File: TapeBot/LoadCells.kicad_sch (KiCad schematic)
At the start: 34 parts, among them Q2 MMBT4403

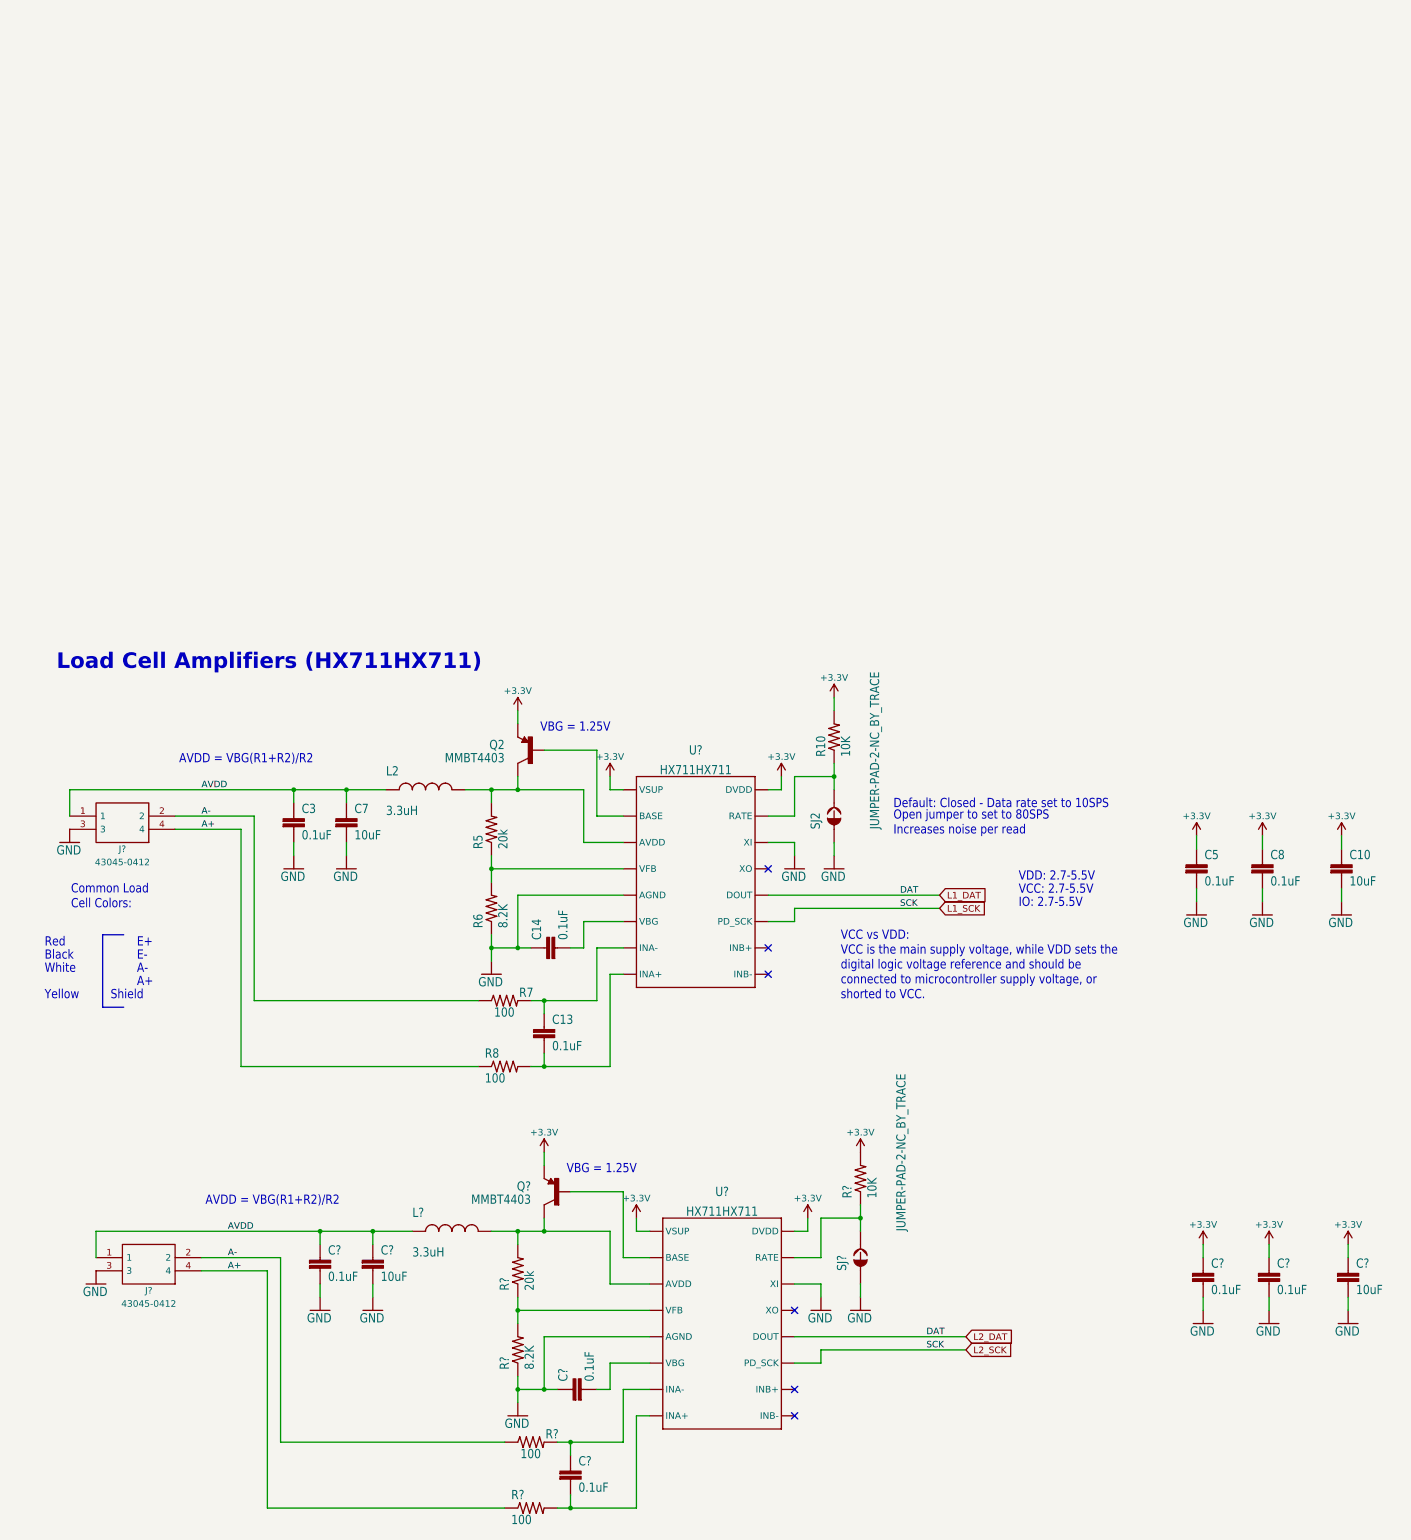
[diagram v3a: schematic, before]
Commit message: fixed footprints and 3d models
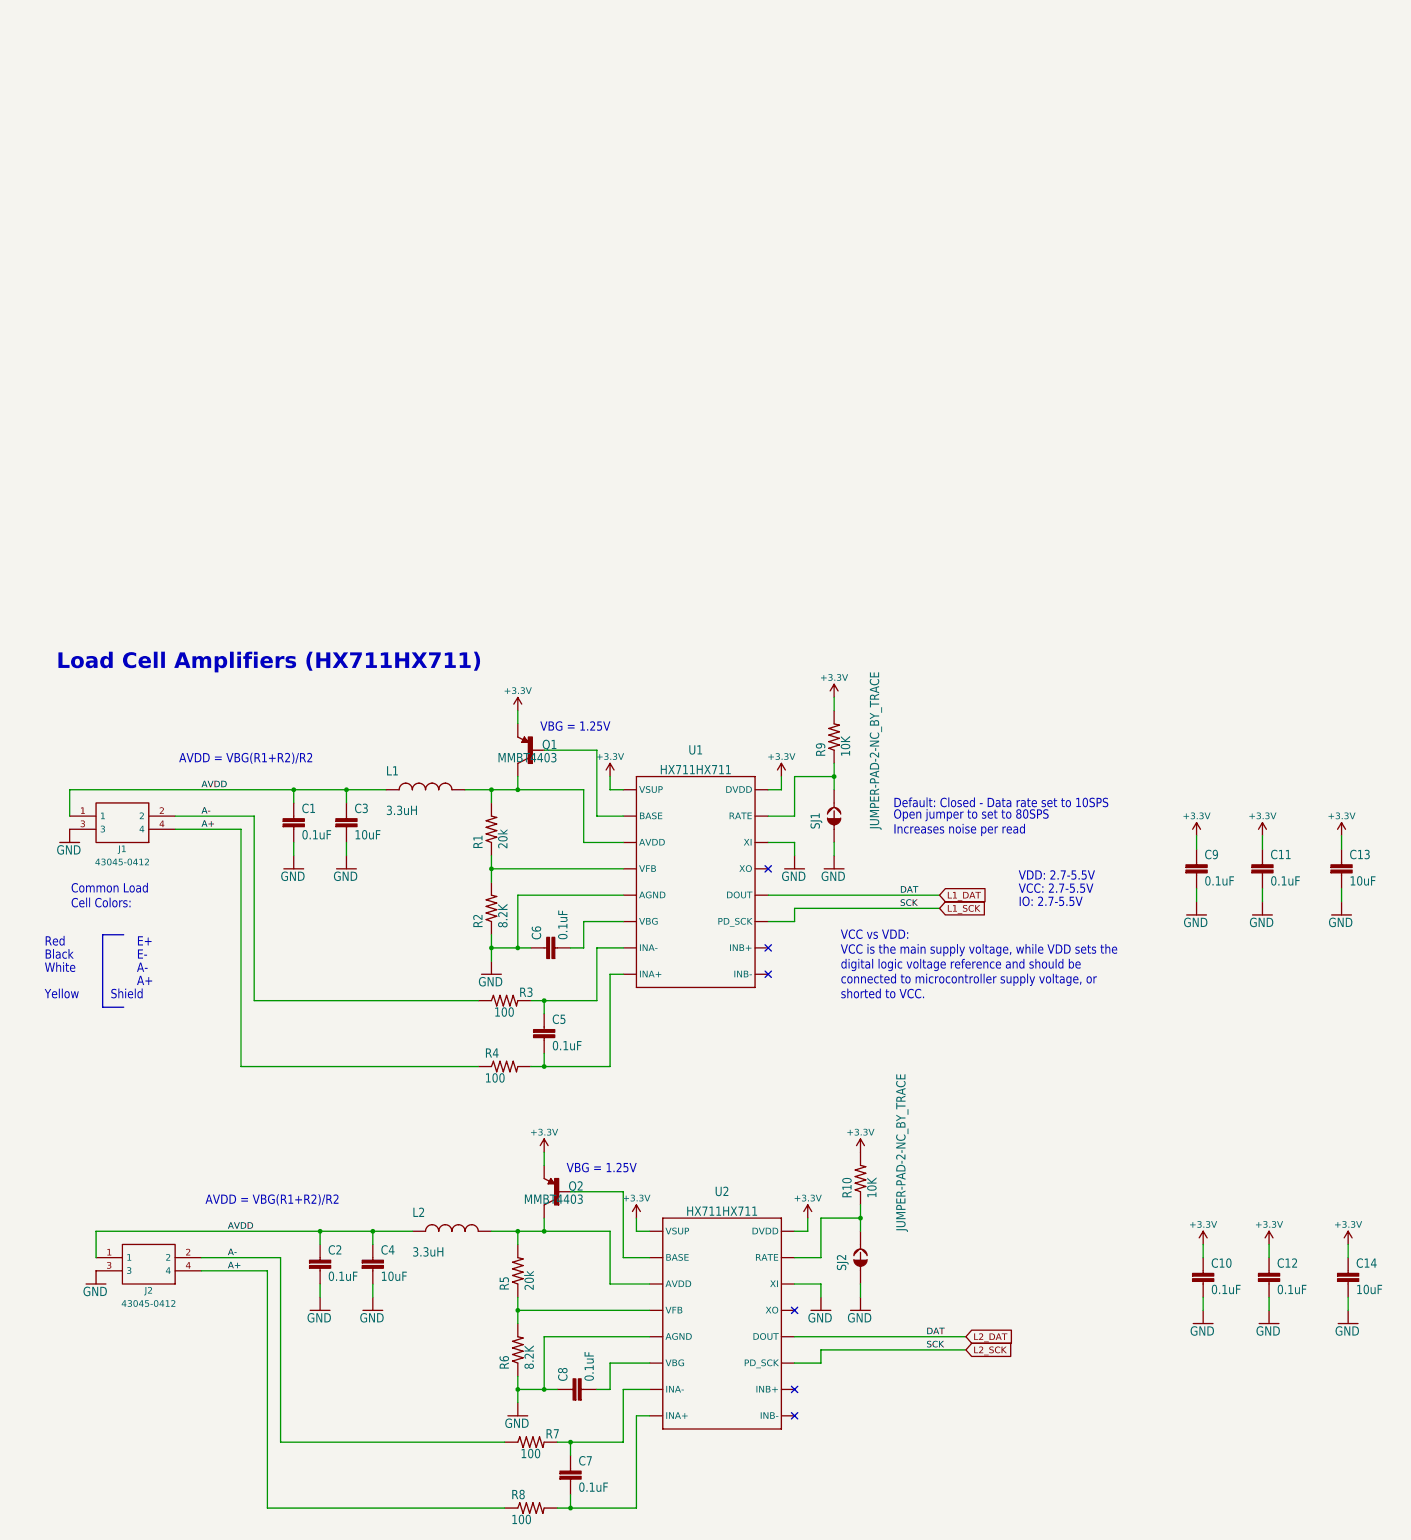
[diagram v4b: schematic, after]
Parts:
- C1: renamed from C3; footprint SparkFun_HX711_Load_Cell:0603-CAP -> Capacitor_SMD:C_0603_1608Metric
- C10, C12, C2, C7, C8: renamed from C?; footprint SparkFun_HX711_Load_Cell:0603-CAP -> Capacitor_SMD:C_0603_1608Metric_Pad1.08x0.95mm_HandSolder
- C11: renamed from C8; footprint SparkFun_HX711_Load_Cell:0603-CAP -> Capacitor_SMD:C_0603_1608Metric_Pad1.08x0.95mm_HandSolder
- C13: renamed from C10; footprint SparkFun_HX711_Load_Cell:1210 -> Capacitor_SMD:C_0805_2012Metric_Pad1.18x1.45mm_HandSolder
- C14, C4: renamed from C?; footprint SparkFun_HX711_Load_Cell:1210 -> Capacitor_SMD:C_0805_2012Metric_Pad1.18x1.45mm_HandSolder
- C3: renamed from C7; footprint SparkFun_HX711_Load_Cell:1210 -> Capacitor_SMD:C_0805_2012Metric_Pad1.18x1.45mm_HandSolder
- C5: renamed from C13; footprint SparkFun_HX711_Load_Cell:0603-CAP -> Capacitor_SMD:C_0603_1608Metric_Pad1.08x0.95mm_HandSolder
- C6: renamed from C14; footprint SparkFun_HX711_Load_Cell:0603-CAP -> Capacitor_SMD:C_0603_1608Metric_Pad1.08x0.95mm_HandSolder
- C9: renamed from C5; footprint SparkFun_HX711_Load_Cell:0603-CAP -> Capacitor_SMD:C_0603_1608Metric_Pad1.08x0.95mm_HandSolder
- L1: renamed from L2; footprint SparkFun_HX711_Load_Cell:0805 -> Capacitor_SMD:C_0805_2012Metric_Pad1.18x1.45mm_HandSolder
- L2: renamed from L?; footprint SparkFun_HX711_Load_Cell:0805 -> Capacitor_SMD:C_0805_2012Metric_Pad1.18x1.45mm_HandSolder
- Q1: renamed from Q2; footprint SparkFun_HX711_Load_Cell:SOT23-3 -> tapebot:SOT23-BEC
- Q2: renamed from Q?; footprint SparkFun_HX711_Load_Cell:SOT23-3 -> tapebot:SOT23-BEC
- R1: renamed from R5; footprint SparkFun_HX711_Load_Cell:0603-RES -> Capacitor_SMD:C_0603_1608Metric_Pad1.08x0.95mm_HandSolder
- R10, R5, R6, R7, R8: renamed from R?; footprint SparkFun_HX711_Load_Cell:0603-RES -> Capacitor_SMD:C_0603_1608Metric_Pad1.08x0.95mm_HandSolder
- R2: renamed from R6; footprint SparkFun_HX711_Load_Cell:0603-RES -> Capacitor_SMD:C_0603_1608Metric_Pad1.08x0.95mm_HandSolder
- R3: renamed from R7; footprint SparkFun_HX711_Load_Cell:0603-RES -> Capacitor_SMD:C_0603_1608Metric_Pad1.08x0.95mm_HandSolder
- R4: renamed from R8; footprint SparkFun_HX711_Load_Cell:0603-RES -> Capacitor_SMD:C_0603_1608Metric_Pad1.08x0.95mm_HandSolder
- R9: renamed from R10; footprint SparkFun_HX711_Load_Cell:0603-RES -> Capacitor_SMD:C_0603_1608Metric_Pad1.08x0.95mm_HandSolder
- SJ1: renamed from SJ2; footprint SparkFun_HX711_Load_Cell:PAD-JUMPER-2-NC_BY_TRACE_YES_SILK -> Jumper:SolderJumper-2_P1.3mm_Open_TrianglePad1.0x1.5mm
- SJ2: renamed from SJ?; footprint SparkFun_HX711_Load_Cell:PAD-JUMPER-2-NC_BY_TRACE_YES_SILK -> Jumper:SolderJumper-2_P1.3mm_Open_TrianglePad1.0x1.5mm
- gave numbers to parts that had none: 4
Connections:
- net +3.3V: now also Q1.E, Q2.E; no longer Q1.2 (E), Q2.2 (E)
- net at L2.2, R5.2, U2.3 (AVDD): now also Q2.C; no longer Q2.3 (C)
- net at U1.2 (BASE): now also Q1.B; no longer Q1.1 (B)
- net at L1.2, R1.2, U1.3 (AVDD): now also Q1.C; no longer Q1.3 (C)
- net at U2.2 (BASE): now also Q2.B; no longer Q2.1 (B)

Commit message: arranged board
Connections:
- net L1_DAT: no longer U2.12 (DOUT)
- net L1_SCK: no longer U2.11 (PD_SCK)
- net A+ renamed 1A+
- net 1A+: no longer J2.4, R8.1
- net A- renamed 1A-
- net 1A-: no longer J2.2, R7.1
- net AVDD renamed AVDD1
- net AVDD1: no longer C2.1, C4.1, J2.1, L2.1
- new net 2A+: J2.4, R8.1
- new net 2A-: J2.2, R7.1
- new net AVDD2: C2.1, C4.1, J2.1, L2.1
- new net L2_DAT: U2.12 (DOUT)
- new net L2_SCK: U2.11 (PD_SCK)
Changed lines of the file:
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@@
     (effects (font (size 1.778 1.5113)) (justify left bottom))
   )
-  (label "A-" (at 55.88 140.97 0)
-    (effects (font (size 1.2446 1.2446)) (justify left bottom))
-  )
-  (label "SCK" (at 190.5 158.75 0)
-    (effects (font (size 1.2446 1.2446)) (justify left bottom))
-  )
-  (label "AVDD" (at 55.88 135.89 0)
-    (effects (font (size 1.2446 1.2446)) (justify left bottom))
-  )
-  (label "SCK" (at 185.42 73.66 0)
-    (effects (font (size 1.2446 1.2446)) (justify left bottom))
-  )
-  (label "A+" (at 55.88 143.51 0)
-    (effects (font (size 1.2446 1.2446)) (justify left bottom))
-  )
-  (label "A+" (at 50.8 58.42 0)
-    (effects (font (size 1.2446 1.2446)) (justify left bottom))
-  )
-  (label "A-" (at 50.8 55.88 0)
-    (effects (font (size 1.2446 1.2446)) (justify left bottom))
-  )
-  (label "DAT" (at 190.5 156.21 0)
-    (effects (font (size 1.2446 1.2446)) (justify left bottom))
-  )
-  (label "AVDD" (at 50.8 50.8 0)
-    (effects (font (size 1.2446 1.2446)) (justify left bottom))
-  )
-  (label "DAT" (at 185.42 71.12 0)
+  (label "2A-" (at 55.88 140.97 0)
+    (effects (font (size 1.2446 1.2446)) (justify left bottom))
+  )
+  (label "2SCK" (at 190.5 158.75 0)
+    (effects (font (size 1.2446 1.2446)) (justify left bottom))
+  )
+  (label "AVDD2" (at 55.88 135.89 0)
+    (effects (font (size 1.2446 1.2446)) (justify left bottom))
+  )
+  (label "1SCK" (at 185.42 73.66 0)
+    (effects (font (size 1.2446 1.2446)) (justify left bottom))
+  )
+  (label "2A+" (at 55.88 143.51 0)
+    (effects (font (size 1.2446 1.2446)) (justify left bottom))
+  )
+  (label "1A+" (at 50.8 58.42 0)
+    (effects (font (size 1.2446 1.2446)) (justify left bottom))
+  )
+  (label "1A-" (at 50.8 55.88 0)
+    (effects (font (size 1.2446 1.2446)) (justify left bottom))
+  )
+  (label "2DAT" (at 190.5 156.21 0)
+    (effects (font (size 1.2446 1.2446)) (justify left bottom))
+  )
+  (label "AVDD1" (at 50.8 50.8 0)
+    (effects (font (size 1.2446 1.2446)) (justify left bottom))
+  )
+  (label "1DAT" (at 185.42 71.12 0)
     (effects (font (size 1.2446 1.2446)) (justify left bottom))
   )
@@
     )
     (pin "B")
+    (pin "C")
     (pin "E")
-    (pin "C")
   )
   (symbol (lib_id "SparkFun_HX711_Load_Cell-eagle-import:GND") (at 243.84 153.67 0) (unit 1)

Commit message: Fixed some footprints
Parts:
- C1: footprint Capacitor_SMD:C_0603_1608Metric -> Capacitor_SMD:C_0603_1608Metric_Pad1.08x0.95mm_HandSolder
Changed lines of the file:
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@@
       (effects (font (size 1.778 1.5113)) (justify left bottom))
     )
-    (property "Footprint" "Capacitor_SMD:C_0603_1608Metric" (id 2) (at 68.58 58.42 0)
+    (property "Footprint" "Capacitor_SMD:C_0603_1608Metric_Pad1.08x0.95mm_HandSolder" (id 2) (at 68.58 58.42 0)
       (effects (font (size 1.27 1.27)) hide)
     )
